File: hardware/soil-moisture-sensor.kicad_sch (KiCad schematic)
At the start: 31 parts, among them J1 USB_B_Micro, Q1 Q_NPN_BEC, Q2 Q_NPN_BEC, SW1 SW_Push, SW2 SW_Push, U2 CP2102N-Axx-xQFN24, U3 ESP32-WROOM-32D

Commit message: re-did a load of routing
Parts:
- added C3: 4.7uF, Capacitor_SMD:C_0603_1608Metric, symbol Device:C
- C1, C4: footprint Capacitor_SMD:C_0201_0603Metric -> Capacitor_SMD:C_0603_1608Metric; LCSC (none) -> C694249
- C2: footprint Capacitor_SMD:C_0201_0603Metric -> Capacitor_SMD:C_0603_1608Metric
- C5: value 4.7uF -> (none); footprint Capacitor_SMD:C_0201_0603Metric -> (none); LCSC (none) -> C108342
- C6: value 22uF -> 4.7uF; footprint Capacitor_SMD:C_0805_2012Metric -> Capacitor_SMD:C_0603_1608Metric; LCSC (none) -> C108342
- C7: LCSC (none) -> C694249
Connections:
- net +BATT: now also C3.1
- net GND: now also C3.2
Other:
- moved on the sheet: C7
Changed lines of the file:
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@@
     (comment 2 "Licensed under CERN-OHL-P v2")
   )
+  (junction (at 199.39 26.67) (diameter 0) (color 0 0 0 0)
+  )
   (junction (at 134.62 124.46) (diameter 0) (color 0 0 0 0)
   )
   (junction (at 30.48 143.51) (diameter 0) (color 0 0 0 0)
   )
+  (junction (at 199.39 34.29) (diameter 0) (color 0 0 0 0)
+  )
+  (junction (at 172.72 66.04) (diameter 0) (color 0 0 0 0)
+  )
+  (junction (at 120.65 48.26) (diameter 0) (color 0 0 0 0)
+  )
+  (junction (at 213.36 26.67) (diameter 0) (color 0 0 0 0)
+  )
+  (junction (at 85.09 48.26) (diameter 0) (color 0 0 0 0)
+  )
   (junction (at 205.74 26.67) (diameter 0) (color 0 0 0 0)
   )
-  (junction (at 172.72 66.04) (diameter 0) (color 0 0 0 0)
-  )
-  (junction (at 120.65 48.26) (diameter 0) (color 0 0 0 0)
-  )
-  (junction (at 213.36 26.67) (diameter 0) (color 0 0 0 0)
-  )
-  (junction (at 85.09 48.26) (diameter 0) (color 0 0 0 0)
-  )
   (junction (at 72.39 170.18) (diameter 0) (color 0 0 0 0)
   )
@@
     (stroke (width 0) (type default) (color 0 0 0 0))
   )
+  (wire (pts (xy 191.77 26.67) (xy 199.39 26.67))
+    (stroke (width 0) (type default) (color 0 0 0 0))
+  )
   (wire (pts (xy 228.6 53.34) (xy 231.14 53.34))
     (stroke (width 0) (type default) (color 0 0 0 0))
@@
     (stroke (width 0) (type default) (color 0 0 0 0))
   )
+  (wire (pts (xy 205.74 26.67) (xy 213.36 26.67))
+    (stroke (width 0) (type default) (color 0 0 0 0))
+  )
   (wire (pts (xy 214.63 144.78) (xy 222.25 144.78))
     (stroke (width 0) (type default) (color 0 0 0 0))
@@
     (stroke (width 0) (type default) (color 0 0 0 0))
   )
+  (wire (pts (xy 191.77 34.29) (xy 199.39 34.29))
+    (stroke (width 0) (type default) (color 0 0 0 0))
+  )
   (wire (pts (xy 170.18 104.14) (xy 170.18 106.68))
     (stroke (width 0) (type default) (color 0 0 0 0))
@@
   )
   (wire (pts (xy 53.34 184.15) (xy 53.34 170.18))
-    (stroke (width 0) (type default) (color 0 0 0 0))
-  )
-  (wire (pts (xy 205.74 26.67) (xy 213.36 26.67))
     (stroke (width 0) (type default) (color 0 0 0 0))
   )
@@
       (effects (font (size 1.27 1.27)) (justify left))
     )
-    (property "Footprint" "Capacitor_SMD:C_0201_0603Metric" (id 2) (at 73.3552 182.88 0)
+    (property "Footprint" "Capacitor_SMD:C_0603_1608Metric" (id 2) (at 73.3552 182.88 0)
       (effects (font (size 1.27 1.27)) hide)
     )
@@
     (pin "1")
   )
-  (symbol (lib_id "Device:C") (at 199.39 30.48 0) (unit 1)
-    (in_bom yes) (on_board yes)
-    (property "Reference" "C7" (id 0) (at 194.31 27.94 0)
-      (effects (font (size 1.27 1.27)) (justify left))
-    )
-    (property "Value" "0.1uF" (id 1) (at 193.04 33.02 0)
-      (effects (font (size 1.27 1.27)) (justify left))
-    )
-    (property "Footprint" "Capacitor_SMD:C_0603_1608Metric" (id 2) (at 200.3552 34.29 0)
-      (effects (font (size 1.27 1.27)) hide)
-    )
-    (property "Datasheet" "~" (id 3) (at 199.39 30.48 0)
+  (symbol (lib_id "Device:C") (at 191.77 30.48 0) (unit 1)
+    (in_bom yes) (on_board yes)
+    (property "Reference" "C7" (id 0) (at 190.5 25.4 0)
+      (effects (font (size 1.27 1.27)) (justify left))
+    )
+    (property "Value" "0.1uF" (id 1) (at 186.69 35.56 0)
+      (effects (font (size 1.27 1.27)) (justify left))
+    )
+    (property "Footprint" "Capacitor_SMD:C_0603_1608Metric" (id 2) (at 192.7352 34.29 0)
+      (effects (font (size 1.27 1.27)) hide)
+    )
+    (property "Datasheet" "~" (id 3) (at 191.77 30.48 0)
+      (effects (font (size 1.27 1.27)) hide)
+    )
+    (property "LCSC" "C694249 " (id 4) (at 191.77 30.48 0)
       (effects (font (size 1.27 1.27)) hide)
     )
@@
     )
     (property "Datasheet" "~" (id 3) (at 35.56 143.51 0)
+      (effects (font (size 1.27 1.27)) hide)
+    )
+    (pin "1")
+    (pin "2")
+  )
+  (symbol (lib_id "Device:C") (at 199.39 30.48 0) (unit 1)
+    (in_bom yes) (on_board yes)
+    (property "Reference" "C3" (id 0) (at 196.85 25.4 0)
+      (effects (font (size 1.27 1.27)) (justify left))
+    )
+    (property "Value" "4.7uF" (id 1) (at 194.31 35.56 0)
+      (effects (font (size 1.27 1.27)) (justify left))
+    )
+    (property "Footprint" "Capacitor_SMD:C_0603_1608Metric" (id 2) (at 200.3552 34.29 0)
+      (effects (font (size 1.27 1.27)) hide)
+    )
+    (property "Datasheet" "~" (id 3) (at 199.39 30.48 0)
+      (effects (font (size 1.27 1.27)) hide)
+    )
+    (property "LCSC" "C108342 " (id 4) (at 199.39 30.48 0)
       (effects (font (size 1.27 1.27)) hide)
     )
@@
     (pin "2")
   )
+  (symbol (lib_id "Device:C") (at 205.74 30.48 0) (unit 1)
+    (in_bom yes) (on_board yes)
+    (property "Reference" "C6" (id 0) (at 205.74 25.4 0)
+      (effects (font (size 1.27 1.27)) (justify left))
+    )
+    (property "Value" "4.7uF" (id 1) (at 205.74 35.56 0)
+      (effects (font (size 1.27 1.27)) (justify left))
+    )
+    (property "Footprint" "Capacitor_SMD:C_0603_1608Metric" (id 2) (at 206.7052 34.29 0)
+      (effects (font (size 1.27 1.27)) hide)
+    )
+    (property "Datasheet" "~" (id 3) (at 205.74 30.48 0)
+      (effects (font (size 1.27 1.27)) hide)
+    )
+    (property "LCSC" "C108342 " (id 4) (at 205.74 30.48 0)
+      (effects (font (size 1.27 1.27)) hide)
+    )
+    (pin "1")
+    (pin "2")
+  )
   (symbol (lib_id "power:+5V") (at 165.1 100.33 0) (unit 1)
     (in_bom yes) (on_board yes) (fields_autoplaced)
@@
     (pin "1")
   )
-  (symbol (lib_id "Device:C") (at 205.74 30.48 0) (unit 1)
-    (in_bom yes) (on_board yes)
-    (property "Reference" "C6" (id 0) (at 207.01 27.94 0)
-      (effects (font (size 1.27 1.27)) (justify left))
-    )
-    (property "Value" "22uF" (id 1) (at 207.01 33.02 0)
-      (effects (font (size 1.27 1.27)) (justify left))
-    )
-    (property "Footprint" "Capacitor_SMD:C_0805_2012Metric" (id 2) (at 206.7052 34.29 0)
-      (effects (font (size 1.27 1.27)) hide)
-    )
-    (property "Datasheet" "~" (id 3) (at 205.74 30.48 0)
-      (effects (font (size 1.27 1.27)) hide)
-    )
-    (pin "1")
-    (pin "2")
-  )
   (symbol (lib_id "Device:Q_NPN_BEC") (at 50.8 143.51 0) (mirror x) (unit 1)
     (in_bom yes) (on_board yes) (fields_autoplaced)
@@
     (property "Reference" "C1" (id 0) (at 74.93 53.34 90))
     (property "Value" "0.1uF" (id 1) (at 72.39 58.42 90))
-    (property "Footprint" "Capacitor_SMD:C_0201_0603Metric" (id 2) (at 76.2 53.6448 0)
+    (property "Footprint" "Capacitor_SMD:C_0603_1608Metric" (id 2) (at 76.2 53.6448 0)
       (effects (font (size 1.27 1.27)) hide)
     )
     (property "Datasheet" "~" (id 3) (at 72.39 54.61 0)
+      (effects (font (size 1.27 1.27)) hide)
+    )
+    (property "LCSC" "C694249 " (id 4) (at 72.39 54.61 0)
       (effects (font (size 1.27 1.27)) hide)
     )
@@
     (property "Reference" "C4" (id 0) (at 110.49 53.34 90))
     (property "Value" "0.1uF" (id 1) (at 107.95 58.42 90))
-    (property "Footprint" "Capacitor_SMD:C_0201_0603Metric" (id 2) (at 111.76 53.6448 0)
+    (property "Footprint" "Capacitor_SMD:C_0603_1608Metric" (id 2) (at 111.76 53.6448 0)
       (effects (font (size 1.27 1.27)) hide)
     )
     (property "Datasheet" "~" (id 3) (at 107.95 54.61 0)
+      (effects (font (size 1.27 1.27)) hide)
+    )
+    (property "LCSC" "C694249 " (id 4) (at 107.95 54.61 0)
       (effects (font (size 1.27 1.27)) hide)
     )
@@
       (effects (font (size 1.27 1.27)) (justify left))
     )
-    (property "Value" "4.7uF" (id 1) (at 176.53 72.3899 0)
-      (effects (font (size 1.27 1.27)) (justify left))
-    )
-    (property "Footprint" "Capacitor_SMD:C_0201_0603Metric" (id 2) (at 173.6852 74.93 0)
+    (property "Value" "" (id 1) (at 176.53 72.3899 0)
+      (effects (font (size 1.27 1.27)) (justify left))
+    )
+    (property "Footprint" "" (id 2) (at 173.6852 74.93 0)
       (effects (font (size 1.27 1.27)) hide)
     )
     (property "Datasheet" "~" (id 3) (at 172.72 71.12 0)
+      (effects (font (size 1.27 1.27)) hide)
+    )
+    (property "LCSC" "C108342 " (id 4) (at 172.72 71.12 0)
       (effects (font (size 1.27 1.27)) hide)
     )
@@
     )
     (path "/e1da2393-df63-4e7e-b7a4-ce89e3f149fc"
-      (reference "C1") (unit 1) (value "0.1uF") (footprint "Capacitor_SMD:C_0201_0603Metric")
+      (reference "C1") (unit 1) (value "0.1uF") (footprint "Capacitor_SMD:C_0603_1608Metric")
     )
     (path "/00000000-0000-0000-0000-00005f25cca2"
-      (reference "C2") (unit 1) (value "1uF") (footprint "Capacitor_SMD:C_0201_0603Metric")
+      (reference "C2") (unit 1) (value "1uF") (footprint "Capacitor_SMD:C_0603_1608Metric")
+    )
+    (path "/22cb4fa7-4138-4ab3-b7f8-2d25746dd0b8"
+      (reference "C3") (unit 1) (value "4.7uF") (footprint "Capacitor_SMD:C_0603_1608Metric")
     )
     (path "/e96def04-8e6d-44cd-ae43-dd53cec285ed"
-      (reference "C4") (unit 1) (value "0.1uF") (footprint "Capacitor_SMD:C_0201_0603Metric")
+      (reference "C4") (unit 1) (value "0.1uF") (footprint "Capacitor_SMD:C_0603_1608Metric")
     )
     (path "/fbd8cd23-5be8-4e30-9e82-fbba8ef09430"
-      (reference "C5") (unit 1) (value "4.7uF") (footprint "Capacitor_SMD:C_0201_0603Metric")
-    )
-    (path "/dd61e408-7346-40a4-9cb9-99cd36090419"
-      (reference "C6") (unit 1) (value "22uF") (footprint "Capacitor_SMD:C_0805_2012Metric")
+      (reference "C5") (unit 1) (value "4.7uF") (footprint "Capacitor_SMD:C_0603_1608Metric")
+    )
+    (path "/9247e970-aeec-403c-b2fb-5f551d7f1986"
+      (reference "C6") (unit 1) (value "4.7uF") (footprint "Capacitor_SMD:C_0603_1608Metric")
     )
     (path "/127c9f22-e863-4cee-b05b-f2b6ce76c56d"

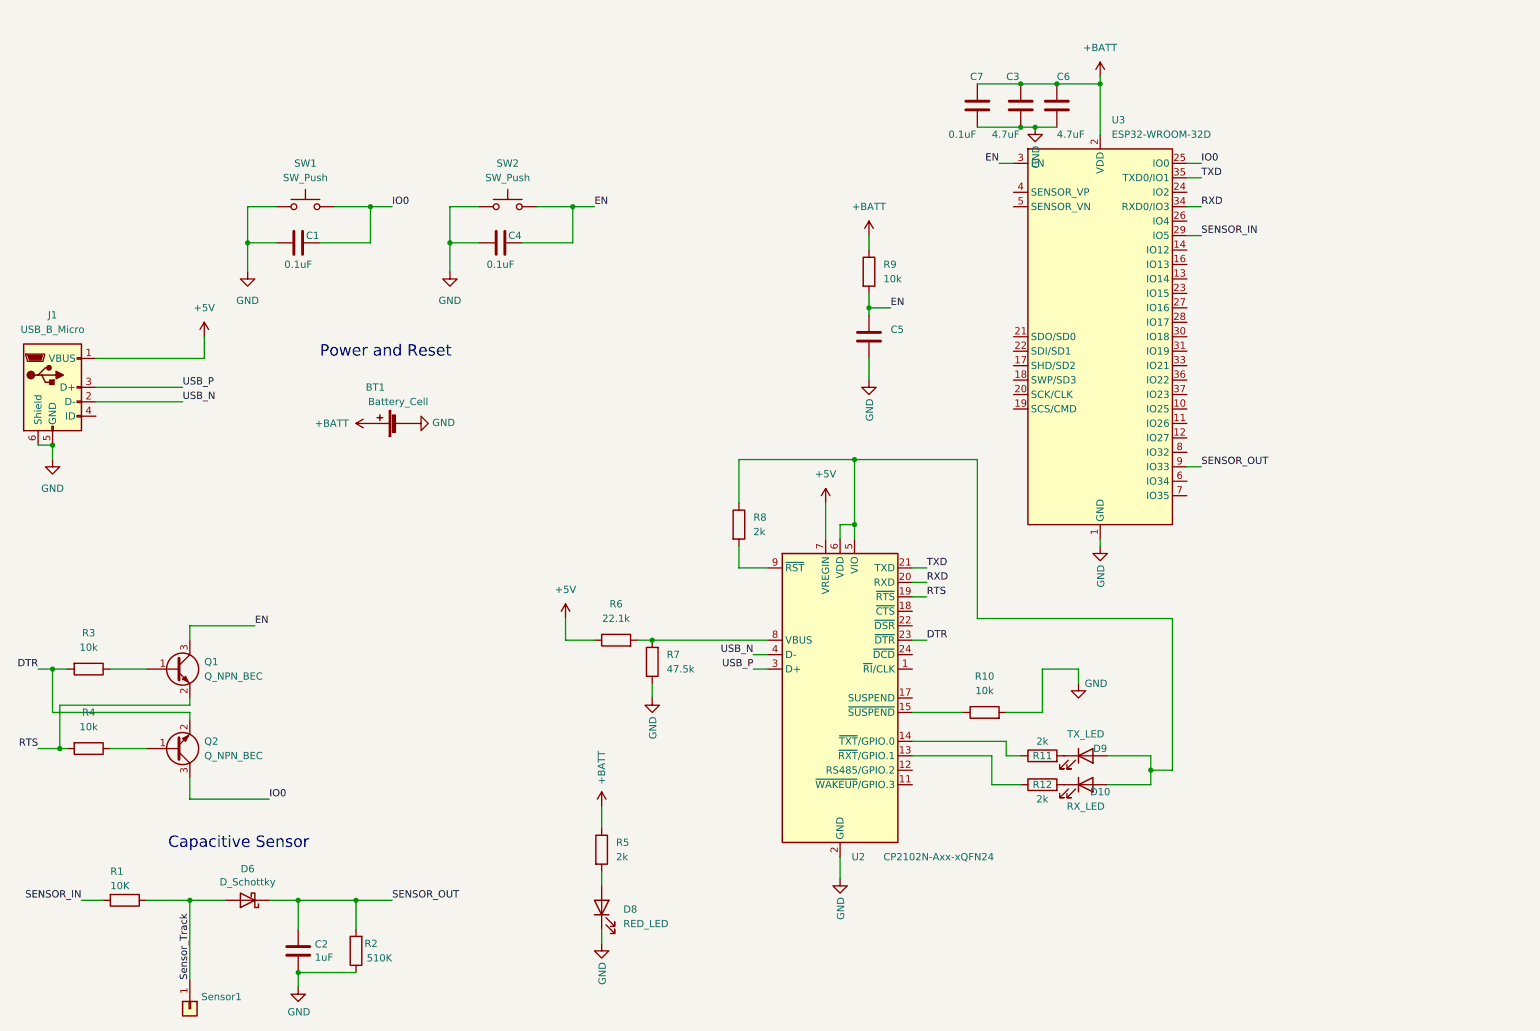
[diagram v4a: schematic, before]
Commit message: added bat mon circuit, made bat led a user led
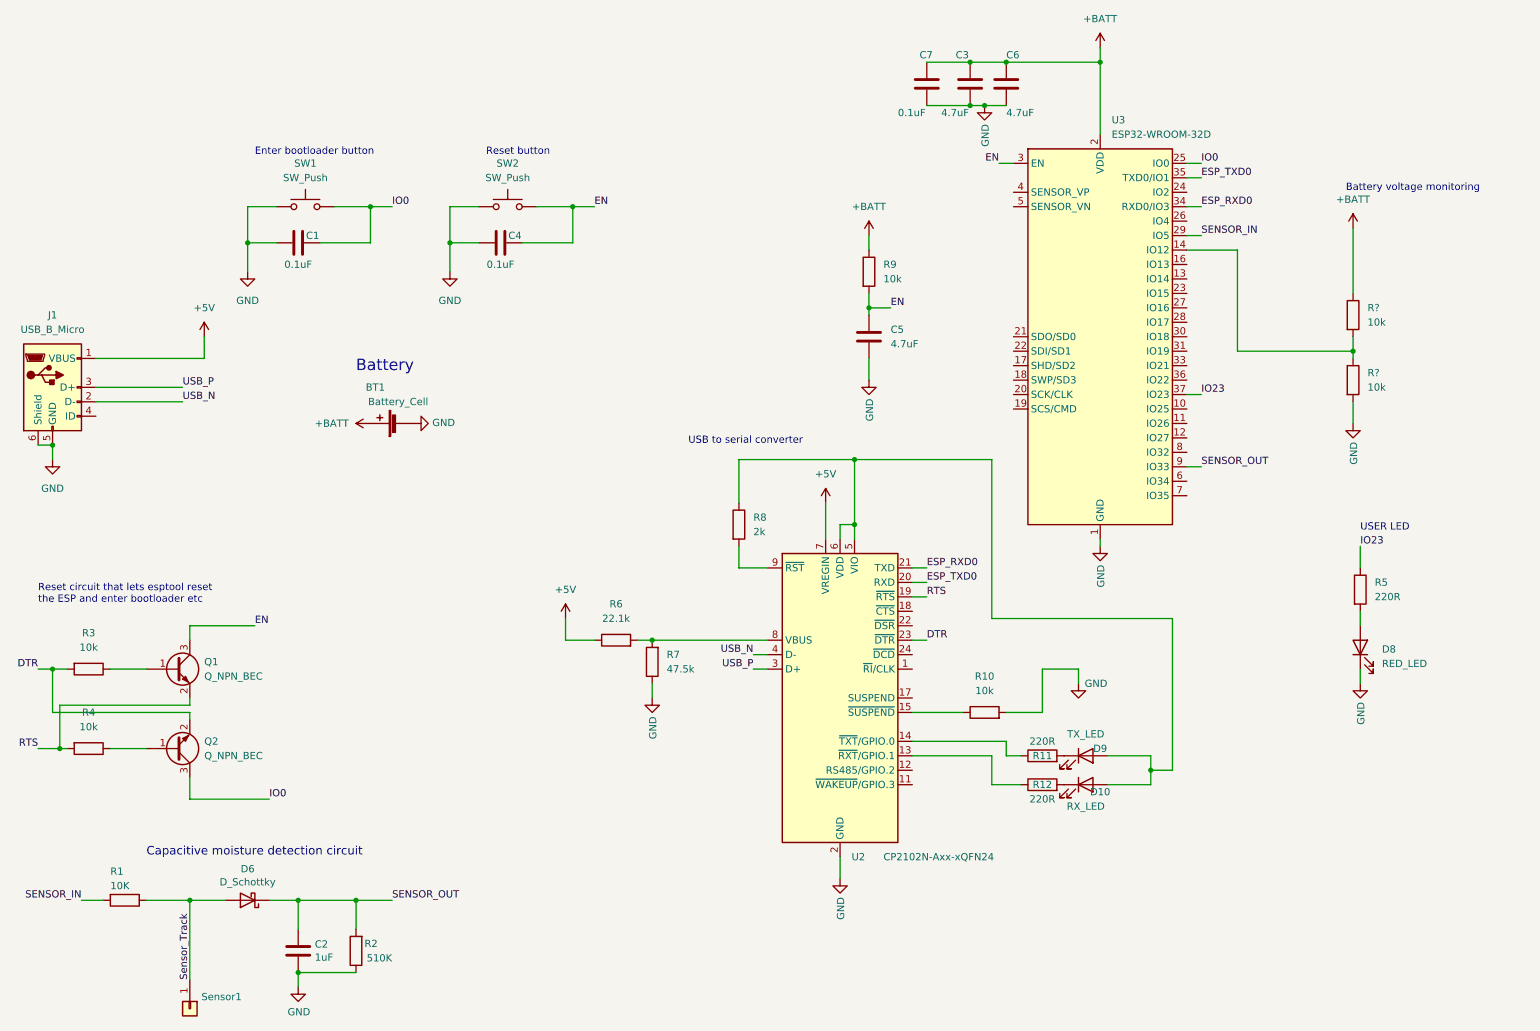
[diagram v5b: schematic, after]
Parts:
- added R? (x2): 10k, Resistor_SMD:R_0603_1608Metric, symbol Device:R
- C5: value (none) -> 4.7uF; footprint (none) -> Capacitor_SMD:C_0603_1608Metric
- D10, D8, D9: LCSC (none) -> C118339
- J1: LCSC (none) -> C132560
- R11, R12: value 2k -> 220R; LCSC (none) -> C365121
- R5: value 2k -> 220R
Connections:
- net +BATT: now also R?.1; no longer R5.1
- net GND: now also R?.2
- net at U3.14 (IO12): now also R?.1, R?.2
- net IO23: now reaches U3.37 (IO23)
- net IO23: now also R5.1
- net RXD renamed ESP_RXD0
- net ESP_RXD0: now also U2.21 (TXD); no longer U2.20 (RXD)
- net TXD renamed ESP_TXD0
- net ESP_TXD0: now also U2.20 (RXD); no longer U2.21 (TXD)
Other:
- note added: "Battery"
- note added: "Battery voltage monitoring"
- note added: "Capacitive moisture detection circuit"
- note added: "Enter bootloader button"
- note added: "Reset button"
- note added: "Reset circuit that lets esptool reset the ESP and enter bootloader etc"
- note added: "USB to serial converter"
- note added: "USER LED"
- note removed: "Capacitive Sensor"
- note removed: "Power and Reset"
- moved on the sheet: C3, C6, C7, D8, R5

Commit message: FIXED SOME DRC ERRORS
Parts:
- gave numbers to parts that had none: 2
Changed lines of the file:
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@@
   (symbol (lib_id "Device:R") (at 257.81 67.31 0) (unit 1)
     (in_bom yes) (on_board yes) (fields_autoplaced)
-    (property "Reference" "R?" (id 0) (at 260.35 66.0399 0)
+    (property "Reference" "R13" (id 0) (at 260.35 66.0399 0)
       (effects (font (size 1.27 1.27)) (justify left))
     )
@@
   (symbol (lib_id "Device:R") (at 257.81 78.74 0) (unit 1)
     (in_bom yes) (on_board yes) (fields_autoplaced)
-    (property "Reference" "R?" (id 0) (at 260.35 77.4699 0)
+    (property "Reference" "R14" (id 0) (at 260.35 77.4699 0)
       (effects (font (size 1.27 1.27)) (justify left))
     )
@@
   (symbol (lib_id "power:+BATT") (at 257.81 52.07 0) (unit 1)
     (in_bom yes) (on_board yes) (fields_autoplaced)
-    (property "Reference" "#PWR?" (id 0) (at 257.81 55.88 0)
+    (property "Reference" "#PWR0114" (id 0) (at 257.81 55.88 0)
       (effects (font (size 1.27 1.27)) hide)
     )
@@
   (symbol (lib_id "power:GND") (at 257.81 86.36 0) (unit 1)
     (in_bom yes) (on_board yes)
-    (property "Reference" "#PWR?" (id 0) (at 257.81 92.71 0)
+    (property "Reference" "#PWR0119" (id 0) (at 257.81 92.71 0)
       (effects (font (size 1.27 1.27)) hide)
     )
@@
       (reference "#PWR0113") (unit 1) (value "GND") (footprint "")
     )
+    (path "/c7da5eb9-5af5-46c6-b3c8-fa78695b7af1"
+      (reference "#PWR0114") (unit 1) (value "+BATT") (footprint "")
+    )
     (path "/f4de557e-7c2f-42b4-8102-bb312c24def0"
       (reference "#PWR0115") (unit 1) (value "+BATT") (footprint "")
@@
       (reference "#PWR0118") (unit 1) (value "GND") (footprint "")
     )
+    (path "/cb503375-0430-4c02-aa2a-a7a0c1a54529"
+      (reference "#PWR0119") (unit 1) (value "GND") (footprint "")
+    )
     (path "/fbc97f02-2202-4d88-8192-ed177178faec"
       (reference "#PWR0120") (unit 1) (value "GND") (footprint "")
     )
-    (path "/c7da5eb9-5af5-46c6-b3c8-fa78695b7af1"
-      (reference "#PWR?") (unit 1) (value "+BATT") (footprint "")
-    )
-    (path "/cb503375-0430-4c02-aa2a-a7a0c1a54529"
-      (reference "#PWR?") (unit 1) (value "GND") (footprint "")
-    )
     (path "/00000000-0000-0000-0000-00005f29204b"
       (reference "BT1") (unit 1) (value "Battery_Cell") (footprint "kicad_footprints:CR123A Battery Holder")
@@
     )
     (path "/079a791d-4be3-4f64-b2b4-2689af465fb0"
-      (reference "R?") (unit 1) (value "10k") (footprint "Resistor_SMD:R_0603_1608Metric")
+      (reference "R13") (unit 1) (value "10k") (footprint "Resistor_SMD:R_0603_1608Metric")
     )
     (path "/7dc2e59d-84c1-4673-a0c3-d287d43e80c1"
-      (reference "R?") (unit 1) (value "10k") (footprint "Resistor_SMD:R_0603_1608Metric")
+      (reference "R14") (unit 1) (value "10k") (footprint "Resistor_SMD:R_0603_1608Metric")
     )
     (path "/3f15063e-257b-49ff-a175-b33019d70662"
